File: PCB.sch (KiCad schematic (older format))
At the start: 46 parts, among them J1 PASSIVE_CHANNELS, J10 USB_RASPBERRY, J11 USB_ARDUINO, J12 100W_ch+, J13 100W_ch-, J14 100W_sense, J2 PASSIVE_CHANNELS, J3 PASSIVE_CHANNELS, J4 12V+, J5 12V-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

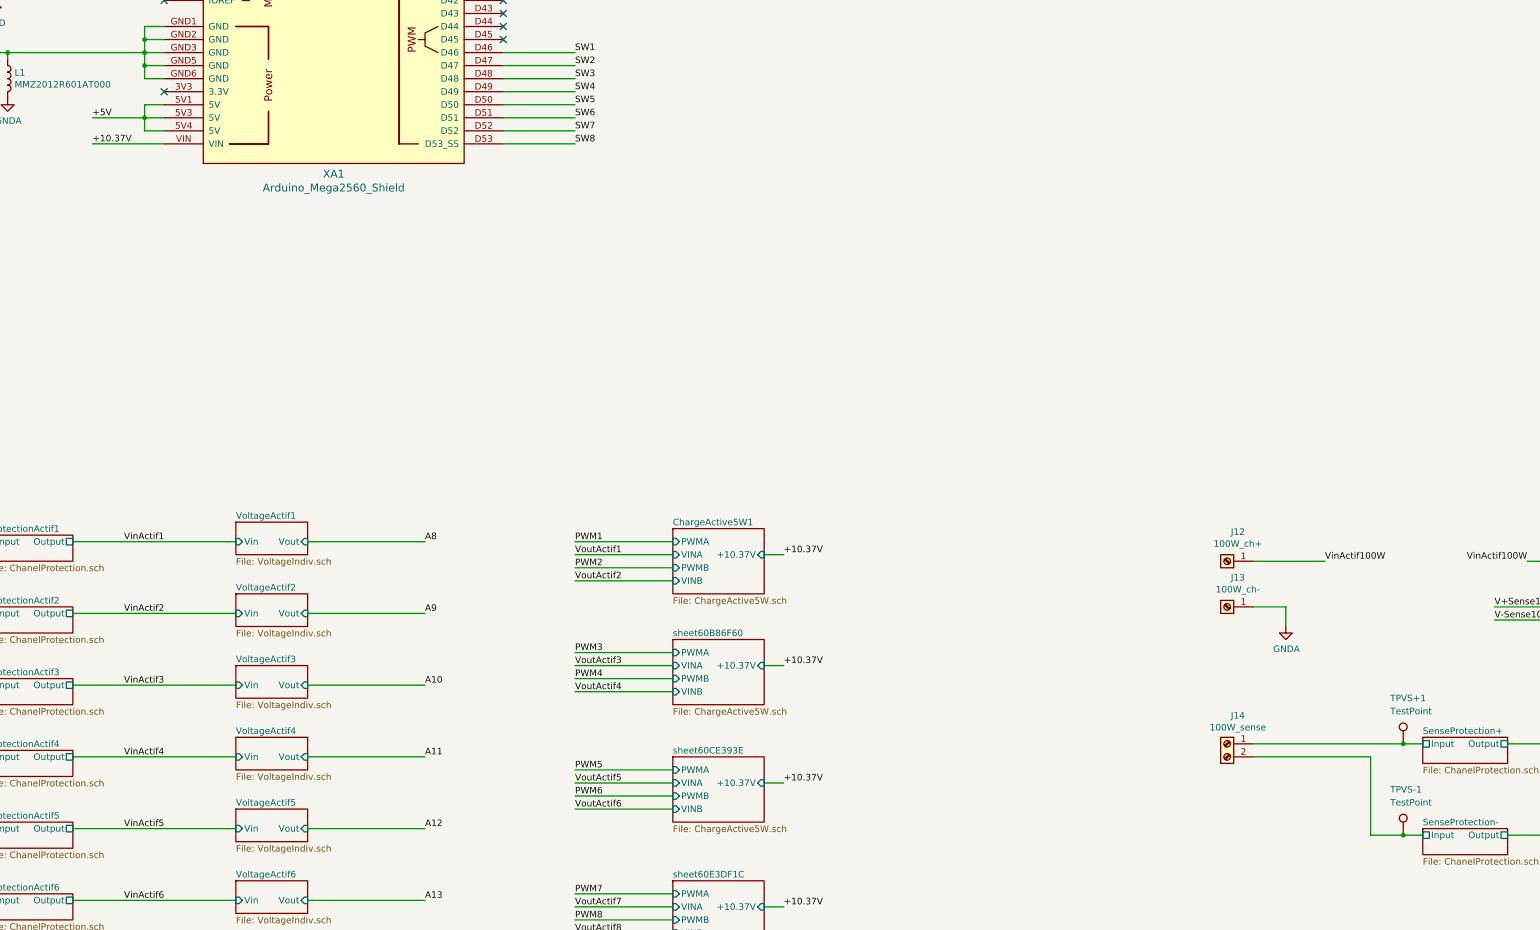
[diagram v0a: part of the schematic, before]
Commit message: routing input canaux voltages
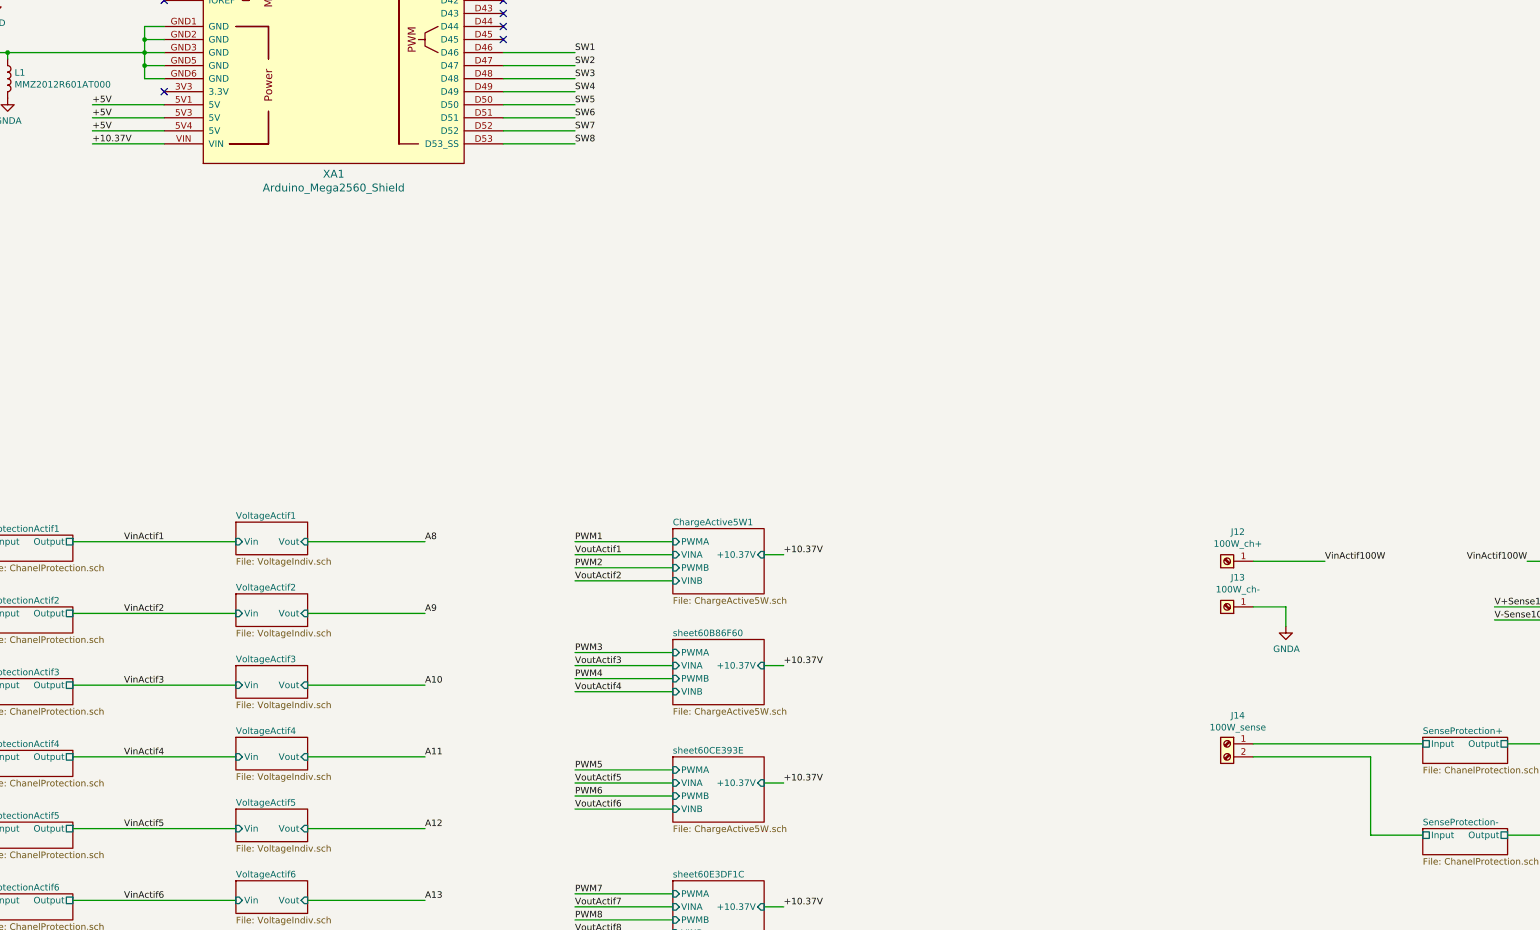
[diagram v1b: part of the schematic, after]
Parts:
- removed TPVS+1, TPVS-1: TestPoint, TestPoint:TestPoint_Pad_1.0x1.0mm, symbol Connector:TestPoint
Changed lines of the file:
@@
 Text Label 4600 2300 0    50   ~ 0
 +5V
-Wire Wire Line
-	19950 12400 19800 12400
 Text Label 19400 12500 0    50   ~ 0
 +5V
@@
 	18550 12000 18550 12050
 Wire Wire Line
-	19800 12500 19950 12500
-Wire Wire Line
-	19800 12400 19800 12500
-Wire Wire Line
-	19800 12500 19800 12600
-Wire Wire Line
-	19800 12600 19950 12600
-Connection ~ 19800 12500
-Wire Wire Line
-	19400 12500 19800 12500
-Wire Wire Line
 	17950 11450 17650 11450
 Wire Wire Line
@@
 F3 "Output" U R 30250 17300 50
 $EndSheet
-$Comp
-L Connector:TestPoint TPVS+?
-U 1 1 5F1340B0
-P 29450 17300
-AR Path="/5EBDFBAE/5F1340B0" Ref="TPVS+?"  Part="1"
-AR Path="/5EC0778F/5F1340B0" Ref="TPVS+?"  Part="1"
-AR Path="/5ECCDD4B/5F1340B0" Ref="TPVS+?"  Part="1"
-AR Path="/5ECD7158/5F1340B0" Ref="TPVS+?"  Part="1"
-AR Path="/5ECE0B35/5F1340B0" Ref="TPVS+?"  Part="1"
-AR Path="/5EC21102/5F1340B0" Ref="TPVS+?"  Part="1"
-AR Path="/5EC2114E/5F1340B0" Ref="TPVS+?"  Part="1"
-AR Path="/5EC2119A/5F1340B0" Ref="TPVS+?"  Part="1"
-AR Path="/5EC211E6/5F1340B0" Ref="TPVS+?"  Part="1"
-AR Path="/5EC536EA/5F1340B0" Ref="TPVS+?"  Part="1"
-AR Path="/5EC60ECA/5F1340B0" Ref="TPVS+?"  Part="1"
-AR Path="/5EC6E362/5F1340B0" Ref="TPVS+?"  Part="1"
-AR Path="/5EC7BA20/5F1340B0" Ref="TPVS+?"  Part="1"
-AR Path="/5EC88F26/5F1340B0" Ref="TPVS+?"  Part="1"
-AR Path="/5EC96422/5F1340B0" Ref="TPVS+?"  Part="1"
-AR Path="/5ECA39A0/5F1340B0" Ref="TPVS+?"  Part="1"
-AR Path="/5F466AC8/5F1340B0" Ref="TPVS+?"  Part="1"
-AR Path="/5F466B4B/5F1340B0" Ref="TPVS+?"  Part="1"
-AR Path="/5F466B56/5F1340B0" Ref="TPVS+?"  Part="1"
-AR Path="/5F466B61/5F1340B0" Ref="TPVS+?"  Part="1"
-AR Path="/5F1340B0" Ref="TPVS+1"  Part="1"
-F 0 "TPVS+1" H 29350 17650 50  0000 L CNN
-F 1 "TestPoint" H 29350 17550 50  0000 L CNN
-F 2 "TestPoint:TestPoint_Pad_1.0x1.0mm" H 29650 17300 50  0001 C CNN
-F 3 "~" H 29650 17300 50  0001 C CNN
-	1    29450 17300
-	1    0    0    -1
-$EndComp
-Wire Wire Line
-	29450 17300 29600 17300
-Wire Wire Line
-	28300 17300 29450 17300
-Connection ~ 29450 17300
 $Sheet
 S 29600 17950 650  200
@@
 F3 "Output" U R 30250 18000 50
 $EndSheet
-$Comp
-L Connector:TestPoint TPVS-?
-U 1 1 5F5525B0
-P 29450 18000
-AR Path="/5EBDFBAE/5F5525B0" Ref="TPVS-?"  Part="1"
-AR Path="/5EC0778F/5F5525B0" Ref="TPVS-?"  Part="1"
-AR Path="/5ECCDD4B/5F5525B0" Ref="TPVS-?"  Part="1"
-AR Path="/5ECD7158/5F5525B0" Ref="TPVS-?"  Part="1"
-AR Path="/5ECE0B35/5F5525B0" Ref="TPVS-?"  Part="1"
-AR Path="/5EC21102/5F5525B0" Ref="TPVS-?"  Part="1"
-AR Path="/5EC2114E/5F5525B0" Ref="TPVS-?"  Part="1"
-AR Path="/5EC2119A/5F5525B0" Ref="TPVS-?"  Part="1"
-AR Path="/5EC211E6/5F5525B0" Ref="TPVS-?"  Part="1"
-AR Path="/5EC536EA/5F5525B0" Ref="TPVS-?"  Part="1"
-AR Path="/5EC60ECA/5F5525B0" Ref="TPVS-?"  Part="1"
-AR Path="/5EC6E362/5F5525B0" Ref="TPVS-?"  Part="1"
-AR Path="/5EC7BA20/5F5525B0" Ref="TPVS-?"  Part="1"
-AR Path="/5EC88F26/5F5525B0" Ref="TPVS-?"  Part="1"
-AR Path="/5EC96422/5F5525B0" Ref="TPVS-?"  Part="1"
-AR Path="/5ECA39A0/5F5525B0" Ref="TPVS-?"  Part="1"
-AR Path="/5F466AC8/5F5525B0" Ref="TPVS-?"  Part="1"
-AR Path="/5F466B4B/5F5525B0" Ref="TPVS-?"  Part="1"
-AR Path="/5F466B56/5F5525B0" Ref="TPVS-?"  Part="1"
-AR Path="/5F466B61/5F5525B0" Ref="TPVS-?"  Part="1"
-AR Path="/5F5525B0" Ref="TPVS-1"  Part="1"
-F 0 "TPVS-1" H 29350 18350 50  0000 L CNN
-F 1 "TestPoint" H 29350 18250 50  0000 L CNN
-F 2 "TestPoint:TestPoint_Pad_1.0x1.0mm" H 29650 18000 50  0001 C CNN
-F 3 "~" H 29650 18000 50  0001 C CNN
-	1    29450 18000
-	1    0    0    -1
-$EndComp
-Wire Wire Line
-	29450 18000 29600 18000
 Wire Wire Line
 	29200 17400 29200 18000
 Wire Wire Line
 	28300 17400 29200 17400
-Connection ~ 29450 18000
 Wire Wire Line
 	30250 17300 31100 17300
@@
 Wire Wire Line
 	30150 16350 30950 16350
-Wire Wire Line
-	29200 18000 29450 18000
 NoConn ~ 22550 10900
 NoConn ~ 22550 11000
@@
 Text Label 24950 3350 0    50   ~ 0
 D-
+Wire Wire Line
+	19400 12500 19950 12500
+Text Label 19400 12600 0    50   ~ 0
++5V
+Wire Wire Line
+	19400 12600 19950 12600
+Text Label 19400 12400 0    50   ~ 0
++5V
+Wire Wire Line
+	19400 12400 19950 12400
+Wire Wire Line
+	28300 17300 29600 17300
+Wire Wire Line
+	29200 18000 29600 18000
 $EndSCHEMATC

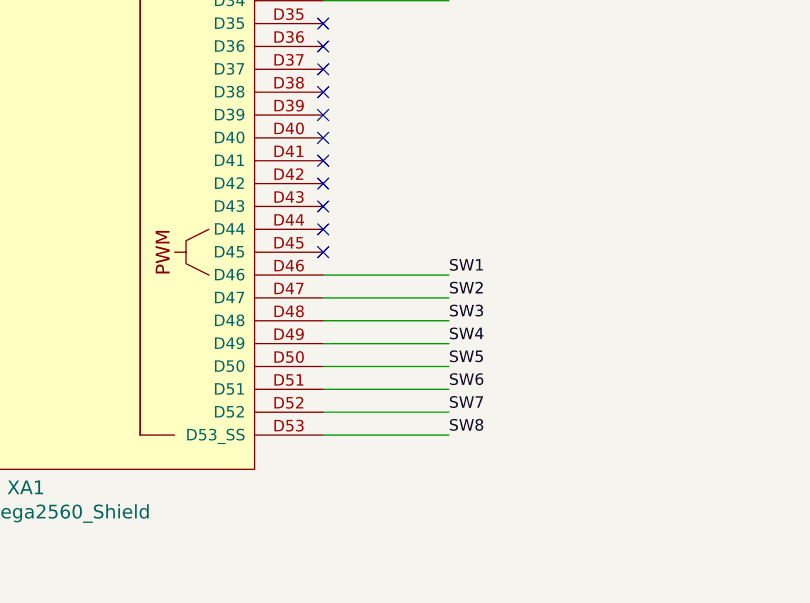
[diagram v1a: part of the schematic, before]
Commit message: Changement pin pour switchs cannaux passifs
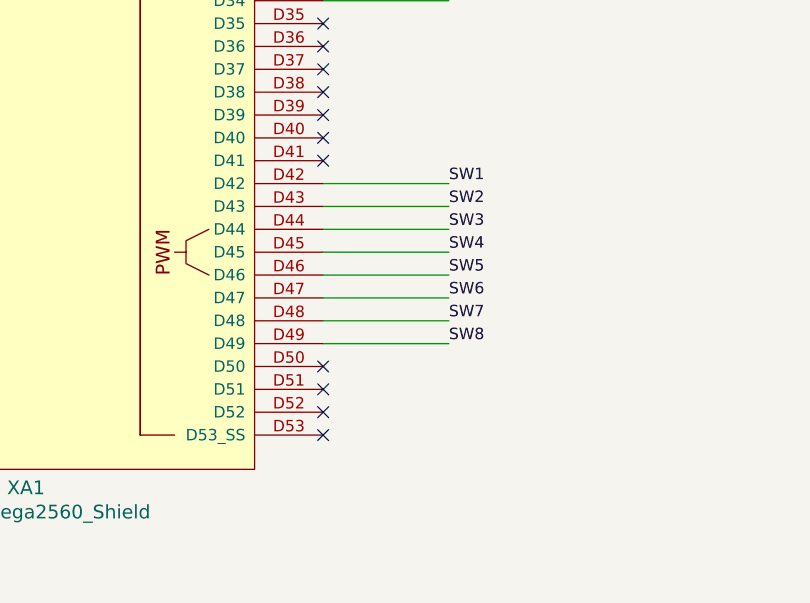
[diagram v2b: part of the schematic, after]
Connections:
- net SW1: now also XA1.D42; no longer XA1.D46
- net SW2: now also XA1.D43; no longer XA1.D47
- net SW3: now also XA1.D44; no longer XA1.D48
- net SW4: now also XA1.D45; no longer XA1.D49
- net SW5: now also XA1.D46; no longer XA1.D50
- net SW6: now also XA1.D47; no longer XA1.D51
- net SW7: now also XA1.D48; no longer XA1.D52
- net SW8: now also XA1.D49; no longer XA1.D53 (D53_SS)
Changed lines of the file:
@@
 RESET
+Wire Wire Line
+	22550 11600 23100 11600
+Text Label 23100 11600 0    50   ~ 0
+SW1
+Wire Wire Line
+	22550 11700 23100 11700
+Text Label 23100 11700 0    50   ~ 0
+SW2
+Wire Wire Line
+	22550 11800 23100 11800
+Text Label 23100 11800 0    50   ~ 0
+SW3
+Wire Wire Line
+	22550 11900 23100 11900
+Text Label 23100 11900 0    50   ~ 0
+SW4
 Wire Wire Line
 	22550 12000 23100 12000
 Text Label 23100 12000 0    50   ~ 0
-SW1
+SW5
 Wire Wire Line
 	22550 12100 23100 12100
-Text Label 23100 12100 0    50   ~ 0
-SW2
 Wire Wire Line
 	22550 12200 23100 12200
 Text Label 23100 12200 0    50   ~ 0
-SW3
+SW7
 Wire Wire Line
 	22550 12300 23100 12300
 Text Label 23100 12300 0    50   ~ 0
-SW4
-Wire Wire Line
-	22550 12400 23100 12400
-Text Label 23100 12400 0    50   ~ 0
-SW5
-Wire Wire Line
-	22550 12500 23100 12500
-Wire Wire Line
-	22550 12600 23100 12600
-Text Label 23100 12600 0    50   ~ 0
-SW7
-Wire Wire Line
-	22550 12700 23100 12700
-Text Label 23100 12700 0    50   ~ 0
 SW8
-Text Label 23100 12500 0    50   ~ 0
+Text Label 23100 12100 0    50   ~ 0
 SW6
 $Sheet
@@
 NoConn ~ 22550 11400
 NoConn ~ 22550 11500
-NoConn ~ 22550 11600
-NoConn ~ 22550 11700
-NoConn ~ 22550 11800
-NoConn ~ 22550 11900
+NoConn ~ 22550 12400
+NoConn ~ 22550 12500
+NoConn ~ 22550 12600
+NoConn ~ 22550 12700
 NoConn ~ 19950 11300
 NoConn ~ 19950 11600

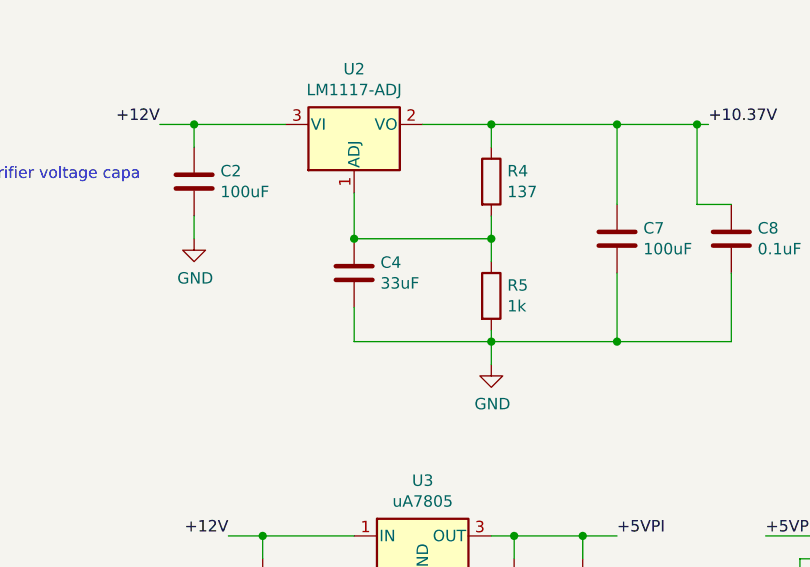
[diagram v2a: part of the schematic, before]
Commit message: Changement valeur de capaciteur + cleanup minime
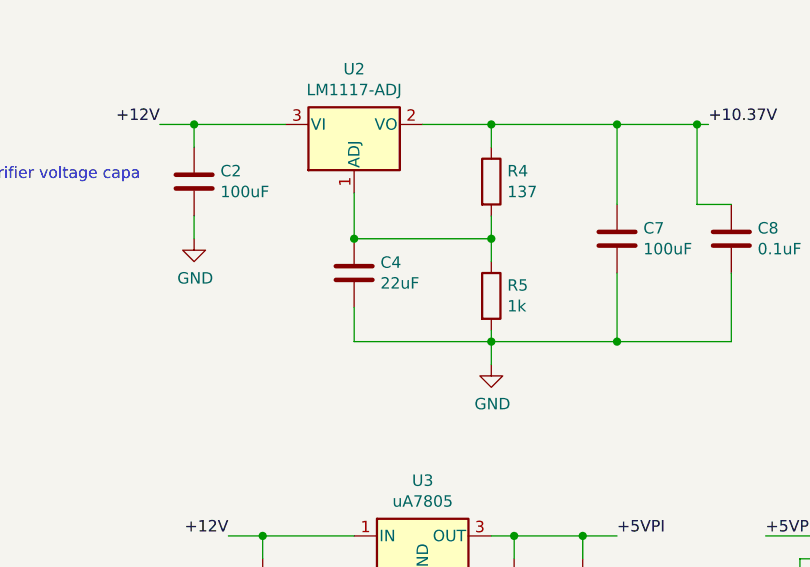
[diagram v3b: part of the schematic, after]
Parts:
- C4: value 33uF -> 22uF
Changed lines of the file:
@@
 P 17050 3300
 F 0 "C4" H 17165 3346 50  0000 L CNN
-F 1 "33uF" H 17165 3255 50  0000 L CNN
+F 1 "22uF" H 17165 3255 50  0000 L CNN
 F 2 "Capacitor_SMD:C_0805_2012Metric" H 17088 3150 50  0001 C CNN
 F 3 "~" H 17050 3300 50  0001 C CNN
